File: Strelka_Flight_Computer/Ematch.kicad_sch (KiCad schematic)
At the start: 16 parts, among them Q10 AP2300, Q11 MMBT2222, Q8 AO3401A, Q9 AO3401A, U15 LM321

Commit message: Started design for V2
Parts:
- removed D9: 1SS388, Diode_SMD:D_SOD-523, symbol Device:D_Schottky_Small_Filled
- removed I2: AL5809-30S1-7, Diode_SMD:D_SOD-123, symbol Simulation_SPICE:IDC
- removed Q8: AO3401A, Package_TO_SOT_SMD:SOT-23, symbol Transistor_FET:AO3401A
- removed R48, R54: 1k, Resistor_SMD:R_0603_1608Metric, symbol Device:R_Small
- removed R52, R69: 100k, Resistor_SMD:R_0603_1608Metric, symbol Device:R_Small
- removed U15: LM321, Package_TO_SOT_SMD:SOT-23-5, symbol Amplifier_Operational:LM321
- added D13: BZT52C3V6T, Diode_SMD:D_SOD-523, symbol Device:D_Zener_Small_Filled
- added R59: 1k, Resistor_SMD:R_0603_1608Metric, symbol Device:R_Small
- added R59: 10k, Resistor_SMD:R_0603_1608Metric, symbol Device:R_Small
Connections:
- net EMATCH+: now also R59.1, R59.2
- net EMATCH_Cont: now also D13.1 (K), R59.1
- net GND: now also D13.2 (A)
- net VDC: now also R59.2

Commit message: Started component placement
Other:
- note removed: "Verify STM32 pins do not do weird shit at boot"
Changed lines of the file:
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@@
     (effects (font (size 2.54 2.54)) (justify left bottom))
-  )
-  (text "Verify STM32 pins do not\ndo weird shit at boot" (at 169.799 71.501 0)
-    (effects (font (size 1.27 1.27)) (justify left bottom))
   )
   (text "Battery \nvoltage \napplied" (at 117.475 40.005 0)

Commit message: Routing starting
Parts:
- removed R49, R50: 100k, Resistor_SMD:R_0603_1608Metric, symbol Device:R_Small
- removed R53, R59: 1k, Resistor_SMD:R_0603_1608Metric, symbol Device:R_Small
- removed R59: 10k, Resistor_SMD:R_0603_1608Metric, symbol Device:R_Small
- added R11, R17: 1k, Resistor_SMD:R_0402_1005Metric, symbol Device:R_Small
- added R15: 10k, Resistor_SMD:R_0402_1005Metric, symbol Device:R_Small
- added R8 (x2): 100k, Resistor_SMD:R_0402_1005Metric, symbol Device:R_Small
- R51: footprint Resistor_SMD:R_0603_1608Metric -> Resistor_SMD:R_0402_1005Metric; LCSC (none) -> C11702
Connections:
- net EMATCH+: now also R15.2, R17.2
- net EMATCH_Cont: now also R15.1
- net FIRE_H: now also R11.1
- net FIRE_L: now also R8.2
- net GND: now also R8.1
- net VDC: now also R17.1, R8.2
- net at Q11.2 (C), Q9.1 (G): now also R8.1
- net at Q11.1 (B): now also R11.2

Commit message: Routing complete
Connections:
- net em+: now reaches Q9.2 (S), R47.2
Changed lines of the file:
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@@
     (stroke (width 0) (type default))
   )
-  (wire (pts (xy 127 43.18) (xy 127 44.45))
+  (wire (pts (xy 127 49.276) (xy 127 49.53))
+    (stroke (width 0) (type default))
+  )
+  (wire (pts (xy 127 43.18) (xy 127 44.196))
     (stroke (width 0) (type default))
   )
@@
     (effects (font (size 2.54 2.54)) (justify left bottom))
   )
+  (label "em+" (at 127 49.403 180) (fields_autoplaced)
+    (effects (font (size 1.27 1.27)) (justify right bottom))
+  )
   (hierarchical_label "FIRE_H" (shape input) (at 157.48 59.69 0) (fields_autoplaced)
     (effects (font (size 1.27 1.27)) (justify left))
@@
     )
   )
-  (symbol (lib_id "Device:R_Small") (at 127 46.99 0) (unit 1)
-    (in_bom yes) (on_board yes) (dnp no) (fields_autoplaced)
-    (property "Reference" "R47" (at 129.54 45.7199 0)
-      (effects (font (size 1.27 1.27)) (justify left))
-    )
-    (property "Value" "2R" (at 129.54 48.2599 0)
-      (effects (font (size 1.27 1.27)) (justify left))
-    )
-    (property "Footprint" "Resistor_SMD:R_2512_6332Metric" (at 127 46.99 0)
-      (effects (font (size 1.27 1.27)) hide)
-    )
-    (property "Datasheet" "https://lcsc.com/product-detail/Chip-span-style-background-color-ff0-Resistor-span-Surface-Mount_UNI-ROYAL-Uniroyal-Elec-HP122WF200KT4E_C91926.html" (at 127 46.99 0)
-      (effects (font (size 1.27 1.27)) hide)
-    )
-    (property "LCSC#" "C91926" (at 127 46.99 0)
-      (effects (font (size 1.27 1.27)) hide)
-    )
+  (symbol (lib_id "Device:R_Small") (at 127 46.736 0) (unit 1)
+    (in_bom yes) (on_board yes) (dnp no) (fields_autoplaced)
+    (property "Reference" "R47" (at 129.54 45.4659 0)
+      (effects (font (size 1.27 1.27)) (justify left))
+    )
+    (property "Value" "2R" (at 129.54 48.0059 0)
+      (effects (font (size 1.27 1.27)) (justify left))
+    )
+    (property "Footprint" "Resistor_SMD:R_2512_6332Metric" (at 127 46.736 0)
+      (effects (font (size 1.27 1.27)) hide)
+    )
+    (property "Datasheet" "https://lcsc.com/product-detail/Chip-span-style-background-color-ff0-Resistor-span-Surface-Mount_UNI-ROYAL-Uniroyal-Elec-HP122WF200KT4E_C91926.html" (at 127 46.736 0)
+      (effects (font (size 1.27 1.27)) hide)
+    )
+    (property "LCSC#" "C91926" (at 127 46.736 0)
+      (effects (font (size 1.27 1.27)) hide)
+    )

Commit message: Created BOM
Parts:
- D13: LCSC (none) -> C2858499; LCSC# C2858499 -> (none)
- Q10: LCSC (none) -> C360338; LCSC# C360338 -> (none)
- Q11: LCSC (none) -> C8512; LCSC# C8512 -> (none)
- Q9: LCSC (none) -> C347476; LCSC# C347476 -> (none)
- R47: LCSC (none) -> C91926; LCSC# C91926 -> (none)
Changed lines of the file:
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@@
       (effects (font (size 1.27 1.27)) (justify left) hide)
     )
-    (property "LCSC#" "C360338" (at 129.54 74.93 0)
+    (property "LCSC" "C360338" (at 129.54 74.93 0)
       (effects (font (size 1.27 1.27)) hide)
     )
@@
       (effects (font (size 1.27 1.27)) hide)
     )
-    (property "LCSC#" "C2858499" (at 139.7 140.462 90)
+    (property "LCSC" "C2858499" (at 139.7 140.462 90)
       (effects (font (size 1.27 1.27)) hide)
     )
@@
       (effects (font (size 1.27 1.27)) (justify left) hide)
     )
-    (property "LCSC#" "C347476" (at 129.54 54.61 0)
+    (property "LCSC" "C347476" (at 129.54 54.61 0)
       (effects (font (size 1.27 1.27)) hide)
     )
@@
       (effects (font (size 1.27 1.27)) hide)
     )
-    (property "LCSC#" "C8512" (at 142.24 59.69 0)
+    (property "LCSC" "C8512" (at 142.24 59.69 0)
       (effects (font (size 1.27 1.27)) hide)
     )
@@
       (effects (font (size 1.27 1.27)) hide)
     )
-    (property "LCSC#" "C91926" (at 127 46.736 0)
-      (effects (font (size 1.27 1.27)) hide)
-    )
+    (property "LCSC" "C91926" (at 127 46.736 0)
+      (effects (font (size 1.27 1.27)) hide)
+    )

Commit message: Started BOM
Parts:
- Q9: LCSC C347476 -> C15127
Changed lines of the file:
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@@
       (effects (font (size 1.27 1.27)) (justify left) hide)
     )
-    (property "LCSC" "C347476" (at 129.54 54.61 0)
+    (property "LCSC" "C15127" (at 129.54 54.61 0)
       (effects (font (size 1.27 1.27)) hide)
     )
+    (property "Field5" "" (at 129.54 54.61 0)
+      (effects (font (size 1.27 1.27)) hide)
+    )

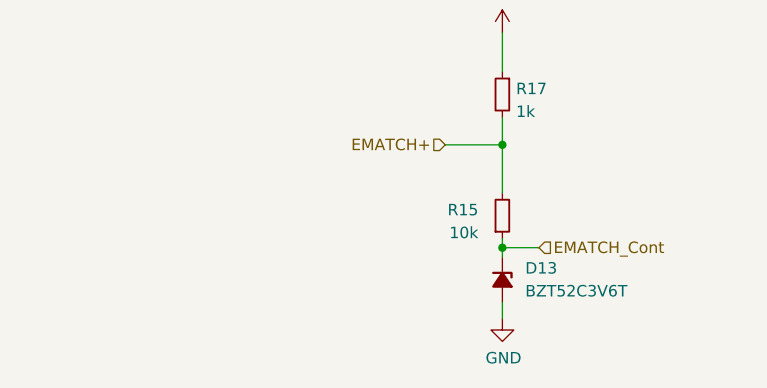
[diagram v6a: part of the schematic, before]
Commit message: Added lp filter caps to adc signals
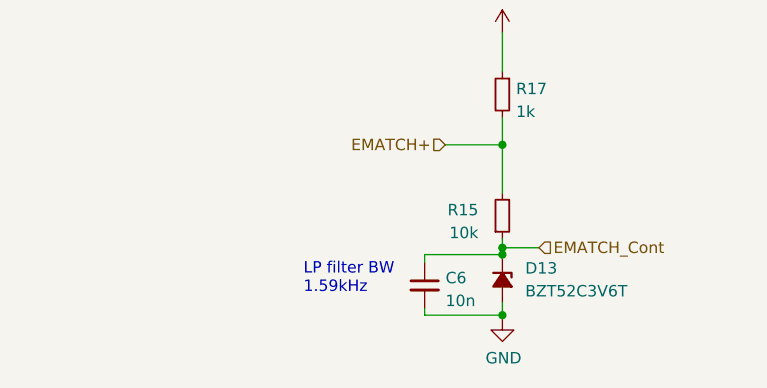
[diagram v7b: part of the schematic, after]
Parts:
- added C6: 10n, Capacitor_SMD:C_0402_1005Metric, symbol Device:C_Small
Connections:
- net EMATCH_Cont: now also C6.1
- net GND: now also C6.2
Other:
- note added: "LP filter BW 1.59kHz"
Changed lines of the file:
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@@
   (junction (at 148.59 74.93) (diameter 0) (color 0 0 0 0)
   )
+  (junction (at 139.7 144.399) (diameter 0) (color 0 0 0 0)
+  )
   (junction (at 139.7 136.906) (diameter 0) (color 0 0 0 0)
   )
   (junction (at 139.7 54.61) (diameter 0) (color 0 0 0 0)
   )
+  (junction (at 139.7 137.668) (diameter 0) (color 0 0 0 0)
+  )
   (wire (pts (xy 139.7 136.906) (xy 143.764 136.906))
     (stroke (width 0) (type default))
@@
     (stroke (width 0) (type default))
   )
+  (wire (pts (xy 139.7 144.399) (xy 139.7 144.78))
+    (stroke (width 0) (type default))
+  )
   (wire (pts (xy 139.7 135.89) (xy 139.7 136.906))
     (stroke (width 0) (type default))
@@
     (stroke (width 0) (type default))
   )
-  (wire (pts (xy 139.7 143.002) (xy 139.7 144.78))
+  (wire (pts (xy 139.7 143.002) (xy 139.7 144.399))
     (stroke (width 0) (type default))
   )
@@
     (stroke (width 0) (type default))
   )
+  (wire (pts (xy 131.064 143.637) (xy 131.064 144.399))
+    (stroke (width 0) (type default))
+  )
   (wire (pts (xy 139.7 113.03) (xy 139.7 117.348))
     (stroke (width 0) (type default))
@@
     (stroke (width 0) (type default))
   )
+  (wire (pts (xy 139.7 137.668) (xy 139.7 137.922))
+    (stroke (width 0) (type default))
+  )
   (wire (pts (xy 156.21 59.69) (xy 157.48 59.69))
     (stroke (width 0) (type default))
   )
+  (wire (pts (xy 131.064 137.668) (xy 139.7 137.668))
+    (stroke (width 0) (type default))
+  )
   (wire (pts (xy 133.35 125.476) (xy 139.7 125.476))
     (stroke (width 0) (type default))
@@
     (stroke (width 0) (type default))
   )
+  (wire (pts (xy 131.064 138.557) (xy 131.064 137.668))
+    (stroke (width 0) (type default))
+  )
   (wire (pts (xy 148.59 74.93) (xy 148.59 76.2))
     (stroke (width 0) (type default))
   )
-  (wire (pts (xy 139.7 136.906) (xy 139.7 137.922))
+  (wire (pts (xy 131.064 144.399) (xy 139.7 144.399))
+    (stroke (width 0) (type default))
+  )
+  (wire (pts (xy 139.7 136.906) (xy 139.7 137.668))
     (stroke (width 0) (type default))
   )
@@
   (text "Ematch Actuation" (at 125.222 33.02 0)
     (effects (font (size 2.54 2.54)) (justify left bottom))
+  )
+  (text "LP filter BW\n1.59kHz" (at 117.602 142.113 0)
+    (effects (font (size 1.27 1.27)) (justify left bottom))
   )
   (label "em+" (at 127 49.403 180) (fields_autoplaced)
@@
         )
       )
+    )
+  )
+  (symbol (lib_id "Device:C_Small") (at 131.064 141.097 0) (unit 1)
+    (in_bom yes) (on_board yes) (dnp no) (fields_autoplaced)
+    (property "Reference" "C6" (at 133.3881 140.2686 0)
+      (effects (font (size 1.27 1.27)) (justify left))
+    )
+    (property "Value" "10n" (at 133.3881 142.8055 0)
+      (effects (font (size 1.27 1.27)) (justify left))
+    )
+    (property "Footprint" "Capacitor_SMD:C_0402_1005Metric" (at 131.064 141.097 0)
+      (effects (font (size 1.27 1.27)) hide)
+    )
+    (property "Datasheet" "~" (at 131.064 141.097 0)
+      (effects (font (size 1.27 1.27)) hide)
+    )
+    (pin "1")
+    (pin "2")
+    (instances
+      (project "Strelka_Flight_Computer"
+        (path "/e63e39d7-6ac0-4ffd-8aa3-1841a4541b55/0daddb18-1491-4767-9ffd-66c8a8ce3cbd"
+          (reference "C6") (unit 1)
+        )
+        (path "/e63e39d7-6ac0-4ffd-8aa3-1841a4541b55/35cf6da3-4352-42df-b1af-73b09ff2e1d9/620b228e-0ce7-49ae-8a03-f7e6e9d55d47"
+          (reference "C12") (unit 1)
+        )
+        (path "/e63e39d7-6ac0-4ffd-8aa3-1841a4541b55/35cf6da3-4352-42df-b1af-73b09ff2e1d9/8cb728ef-7455-4a15-8c69-f1099dedd937"
+          (reference "C13") (unit 1)
+        )
+      )

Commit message: Added LCSC mpn to all relevent parts
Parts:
- R15: LCSC C11702 -> C25744
- R17: LCSC C11702 -> C11702
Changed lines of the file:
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@@
       (effects (font (size 1.27 1.27)) hide)
     )
-    (property "LCSC" "C11702" (at 139.7 119.888 90)
+    (property "LCSC" " C11702" (at 139.7 119.888 90)
       (effects (font (size 1.27 1.27)) hide)
     )
@@
       (effects (font (size 1.27 1.27)) hide)
     )
-    (property "LCSC" "C11702" (at 139.7 133.35 90)
-      (effects (font (size 1.27 1.27)) hide)
-    )
+    (property "LCSC" "C25744" (at 139.7 133.35 90)
+      (effects (font (size 1.27 1.27)) hide)
+    )
